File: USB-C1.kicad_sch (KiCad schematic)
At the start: 24 parts, among them J2 USB_C_Receptacle, J3 I2C_HD3SS3220, U3 HD3SS3220IRNHR, U4 TPS2068EDBVR, U5 TPD4E02B04DQA, U6 TPD4E02B04DQA, U7 TPD4E02B04DQA

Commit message: TPS25762 EEPROM connector added
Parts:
- renumbered R11 to R10, R12 to R11, R8 to R7, R9 to R8, R10 to R9
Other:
- title: (none) -> USB Hub
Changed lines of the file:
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@@
 	(generator_version "9.0")
 	(paper "A4")
+	(title_block
+		(title "USB Hub")
+	)
 	(rectangle
 		(start 15.24 13.97)
@@
 		(on_board yes)
 		(dnp no)
-		(property "Reference" "#PWR053"
+		(property "Reference" "#PWR052"
 			(at 184.15 162.56 0)
 			(effects
@@
 			(project "USB_hub"
 				(path "/a2586c28-95f1-49e6-9254-37d7a8473e53/9818f2bb-7888-47ed-88c0-ae123f59f09a"
-					(reference "#PWR053")
+					(reference "#PWR052")
 					(unit 1)
 				)
@@
 		(dnp no)
 		(fields_autoplaced yes)
-		(property "Reference" "#PWR041"
+		(property "Reference" "#PWR040"
 			(at 149.86 58.42 0)
 			(effects
@@
 			(project ""
 				(path "/a2586c28-95f1-49e6-9254-37d7a8473e53/9818f2bb-7888-47ed-88c0-ae123f59f09a"
-					(reference "#PWR041")
+					(reference "#PWR040")
 					(unit 1)
 				)
@@
 		(dnp no)
 		(fields_autoplaced yes)
-		(property "Reference" "R8"
+		(property "Reference" "R7"
 			(at 50.8 44.4499 0)
 			(effects
@@
 			(project ""
 				(path "/a2586c28-95f1-49e6-9254-37d7a8473e53/9818f2bb-7888-47ed-88c0-ae123f59f09a"
-					(reference "R8")
+					(reference "R7")
 					(unit 1)
 				)
@@
 		(dnp no)
 		(fields_autoplaced yes)
-		(property "Reference" "#PWR056"
+		(property "Reference" "#PWR055"
 			(at 25.4 194.31 0)
 			(effects
@@
 			(project "USB_hub"
 				(path "/a2586c28-95f1-49e6-9254-37d7a8473e53/9818f2bb-7888-47ed-88c0-ae123f59f09a"
-					(reference "#PWR056")
+					(reference "#PWR055")
 					(unit 1)
 				)
@@
 		(dnp no)
 		(fields_autoplaced yes)
-		(property "Reference" "#PWR047"
+		(property "Reference" "#PWR046"
 			(at 26.67 129.54 0)
 			(effects
@@
 			(project ""
 				(path "/a2586c28-95f1-49e6-9254-37d7a8473e53/9818f2bb-7888-47ed-88c0-ae123f59f09a"
-					(reference "#PWR047")
+					(reference "#PWR046")
 					(unit 1)
 				)
@@
 		(dnp no)
 		(fields_autoplaced yes)
-		(property "Reference" "#PWR037"
+		(property "Reference" "#PWR036"
 			(at 26.67 44.45 0)
 			(effects
@@
 			(project ""
 				(path "/a2586c28-95f1-49e6-9254-37d7a8473e53/9818f2bb-7888-47ed-88c0-ae123f59f09a"
-					(reference "#PWR037")
+					(reference "#PWR036")
 					(unit 1)
 				)
@@
 		(dnp no)
 		(fields_autoplaced yes)
-		(property "Reference" "#PWR040"
+		(property "Reference" "#PWR039"
 			(at 57.15 49.53 0)
 			(effects
@@
 			(project ""
 				(path "/a2586c28-95f1-49e6-9254-37d7a8473e53/9818f2bb-7888-47ed-88c0-ae123f59f09a"
-					(reference "#PWR040")
+					(reference "#PWR039")
 					(unit 1)
 				)
@@
 		(dnp no)
 		(fields_autoplaced yes)
-		(property "Reference" "R9"
+		(property "Reference" "R8"
 			(at 43.18 49.53 90)
 			(effects
@@
 			(project ""
 				(path "/a2586c28-95f1-49e6-9254-37d7a8473e53/9818f2bb-7888-47ed-88c0-ae123f59f09a"
-					(reference "R9")
+					(reference "R8")
 					(unit 1)
 				)
@@
 		(dnp no)
 		(fields_autoplaced yes)
-		(property "Reference" "#PWR055"
+		(property "Reference" "#PWR054"
 			(at 262.89 163.83 0)
 			(effects
@@
 			(project "USB_hub"
 				(path "/a2586c28-95f1-49e6-9254-37d7a8473e53/9818f2bb-7888-47ed-88c0-ae123f59f09a"
-					(reference "#PWR055")
+					(reference "#PWR054")
 					(unit 1)
 				)
@@
 		(dnp no)
 		(fields_autoplaced yes)
-		(property "Reference" "#PWR038"
+		(property "Reference" "#PWR037"
 			(at 62.23 44.45 0)
 			(effects
@@
 			(project ""
 				(path "/a2586c28-95f1-49e6-9254-37d7a8473e53/9818f2bb-7888-47ed-88c0-ae123f59f09a"
-					(reference "#PWR038")
+					(reference "#PWR037")
 					(unit 1)
 				)
@@
 		(dnp no)
 		(fields_autoplaced yes)
-		(property "Reference" "#PWR039"
+		(property "Reference" "#PWR038"
 			(at 48.26 45.72 0)
 			(effects
@@
 			(project "USB_hub"
 				(path "/a2586c28-95f1-49e6-9254-37d7a8473e53/9818f2bb-7888-47ed-88c0-ae123f59f09a"
-					(reference "#PWR039")
+					(reference "#PWR038")
 					(unit 1)
 				)
@@
 		(dnp no)
 		(fields_autoplaced yes)
-		(property "Reference" "#PWR051"
+		(property "Reference" "#PWR050"
 			(at 73.66 143.51 0)
 			(effects
@@
 			(project ""
 				(path "/a2586c28-95f1-49e6-9254-37d7a8473e53/9818f2bb-7888-47ed-88c0-ae123f59f09a"
-					(reference "#PWR051")
+					(reference "#PWR050")
 					(unit 1)
 				)
@@
 		(dnp no)
 		(fields_autoplaced yes)
-		(property "Reference" "#PWR045"
+		(property "Reference" "#PWR044"
 			(at 135.89 95.25 0)
 			(effects
@@
 			(project ""
 				(path "/a2586c28-95f1-49e6-9254-37d7a8473e53/9818f2bb-7888-47ed-88c0-ae123f59f09a"
-					(reference "#PWR045")
+					(reference "#PWR044")
 					(unit 1)
 				)
@@
 		(dnp no)
 		(fields_autoplaced yes)
-		(property "Reference" "#PWR035"
+		(property "Reference" "#PWR034"
 			(at 26.67 27.94 0)
 			(effects
@@
 			(project "USB_hub"
 				(path "/a2586c28-95f1-49e6-9254-37d7a8473e53/9818f2bb-7888-47ed-88c0-ae123f59f09a"
-					(reference "#PWR035")
+					(reference "#PWR034")
 					(unit 1)
 				)
@@
 		(dnp no)
 		(fields_autoplaced yes)
-		(property "Reference" "#PWR046"
+		(property "Reference" "#PWR045"
 			(at 248.92 100.33 0)
 			(effects
@@
 			(project ""
 				(path "/a2586c28-95f1-49e6-9254-37d7a8473e53/9818f2bb-7888-47ed-88c0-ae123f59f09a"
-					(reference "#PWR046")
+					(reference "#PWR045")
 					(unit 1)
 				)
@@
 		(on_board yes)
 		(dnp no)
-		(property "Reference" "R11"
+		(property "Reference" "R10"
 			(at 45.212 69.596 90)
 			(effects
@@
 			(project ""
 				(path "/a2586c28-95f1-49e6-9254-37d7a8473e53/9818f2bb-7888-47ed-88c0-ae123f59f09a"
-					(reference "R11")
+					(reference "R10")
 					(unit 1)
 				)
@@
 		(on_board yes)
 		(dnp no)
-		(property "Reference" "#PWR043"
+		(property "Reference" "#PWR042"
 			(at 49.53 59.69 0)
 			(effects
@@
 			(project "USB_hub"
 				(path "/a2586c28-95f1-49e6-9254-37d7a8473e53/9818f2bb-7888-47ed-88c0-ae123f59f09a"
-					(reference "#PWR043")
+					(reference "#PWR042")
 					(unit 1)
 				)
@@
 		(dnp no)
 		(fields_autoplaced yes)
-		(property "Reference" "#PWR036"
+		(property "Reference" "#PWR035"
 			(at 228.6 27.94 0)
 			(effects
@@
 			(project ""
 				(path "/a2586c28-95f1-49e6-9254-37d7a8473e53/9818f2bb-7888-47ed-88c0-ae123f59f09a"
-					(reference "#PWR036")
+					(reference "#PWR035")
 					(unit 1)
 				)
@@
 		(dnp no)
 		(fields_autoplaced yes)
-		(property "Reference" "#PWR054"
+		(property "Reference" "#PWR053"
 			(at 222.25 163.83 0)
 			(effects
@@
 			(project "USB_hub"
 				(path "/a2586c28-95f1-49e6-9254-37d7a8473e53/9818f2bb-7888-47ed-88c0-ae123f59f09a"
-					(reference "#PWR054")
+					(reference "#PWR053")
 					(unit 1)
 				)
@@
 		(dnp no)
 		(fields_autoplaced yes)
-		(property "Reference" "#PWR049"
+		(property "Reference" "#PWR048"
 			(at 26.67 142.24 0)
 			(effects
@@
 			(project "USB_hub"
 				(path "/a2586c28-95f1-49e6-9254-37d7a8473e53/9818f2bb-7888-47ed-88c0-ae123f59f09a"
-					(reference "#PWR049")
+					(reference "#PWR048")
 					(unit 1)
 				)
@@
 		(dnp no)
 		(fields_autoplaced yes)
-		(property "Reference" "R12"
+		(property "Reference" "R11"
 			(at 78.74 130.8099 0)
 			(effects
@@
 			(project ""
 				(path "/a2586c28-95f1-49e6-9254-37d7a8473e53/9818f2bb-7888-47ed-88c0-ae123f59f09a"
-					(reference "R12")
+					(reference "R11")
 					(unit 1)
 				)
@@
 		(on_board yes)
 		(dnp no)
-		(property "Reference" "R10"
+		(property "Reference" "R9"
 			(at 45.212 64.516 90)
 			(effects
@@
 			(project "USB_hub"
 				(path "/a2586c28-95f1-49e6-9254-37d7a8473e53/9818f2bb-7888-47ed-88c0-ae123f59f09a"
-					(reference "R10")
+					(reference "R9")
 					(unit 1)
 				)
@@
 		(on_board yes)
 		(dnp no)
-		(property "Reference" "#PWR042"
+		(property "Reference" "#PWR041"
 			(at 36.83 57.15 0)
 			(effects
@@
 			(project ""
 				(path "/a2586c28-95f1-49e6-9254-37d7a8473e53/9818f2bb-7888-47ed-88c0-ae123f59f09a"
-					(reference "#PWR042")
+					(reference "#PWR041")
 					(unit 1)
 				)
@@
 		(dnp no)
 		(fields_autoplaced yes)
-		(property "Reference" "#PWR044"
+		(property "Reference" "#PWR043"
 			(at 38.1 73.66 0)
 			(effects
@@
 			(project "USB_hub"
 				(path "/a2586c28-95f1-49e6-9254-37d7a8473e53/9818f2bb-7888-47ed-88c0-ae123f59f09a"
-					(reference "#PWR044")
+					(reference "#PWR043")
 					(unit 1)
 				)
@@
 		(dnp no)
 		(fields_autoplaced yes)
-		(property "Reference" "#PWR050"
+		(property "Reference" "#PWR049"
 			(at 36.83 142.24 0)
 			(effects
@@
 			(project "USB_hub"
 				(path "/a2586c28-95f1-49e6-9254-37d7a8473e53/9818f2bb-7888-47ed-88c0-ae123f59f09a"
-					(reference "#PWR050")
+					(reference "#PWR049")
 					(unit 1)
 				)
@@
 		(dnp no)
 		(fields_autoplaced yes)
-		(property "Reference" "#PWR052"
+		(property "Reference" "#PWR051"
 			(at 91.44 143.51 0)
 			(effects
@@
 			(project "USB_hub"
 				(path "/a2586c28-95f1-49e6-9254-37d7a8473e53/9818f2bb-7888-47ed-88c0-ae123f59f09a"
-					(reference "#PWR052")
+					(reference "#PWR051")
 					(unit 1)
 				)
@@
 		(dnp no)
 		(fields_autoplaced yes)
-		(property "Reference" "#PWR048"
+		(property "Reference" "#PWR047"
 			(at 91.44 133.35 0)
 			(effects
@@
 			(project "USB_hub"
 				(path "/a2586c28-95f1-49e6-9254-37d7a8473e53/9818f2bb-7888-47ed-88c0-ae123f59f09a"
-					(reference "#PWR048")
+					(reference "#PWR047")
 					(unit 1)
 				)

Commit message: deleted duplicated capacitor
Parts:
- C22, C28, C30: footprint (none) -> Capacitor_THT:C_Radial_D10.0mm_H16.0mm_P5.00mm
- C23, C24, C25, C26, C27, C29: footprint (none) -> Capacitor_SMD:C_0402_1005Metric
- J2: footprint (none) -> Connector_USB:USB_C_Receptacle_Amphenol_12401610E4-2A
- J3: footprint (none) -> Connector_PinHeader_1.27mm:PinHeader_1x03_P1.27mm_Vertical
- JP1: footprint (none) -> Jumper:SolderJumper-2_P1.3mm_Open_Pad1.0x1.5mm
- R10, R11, R7, R8, R9: footprint (none) -> Resistor_SMD:R_0603_1608Metric
- TP1, TP2: footprint (none) -> TestPoint:TestPoint_2Pads_Pitch5.08mm_Drill1.3mm
- U3: footprint RNH0030A -> footprints:RNH0030A
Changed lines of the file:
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@@
 			)
 		)
-		(property "Footprint" ""
+		(property "Footprint" "Capacitor_SMD:C_0402_1005Metric"
 			(at 134.62 60.96 0)
 			(effects
@@
 			)
 		)
-		(property "Footprint" ""
+		(property "Footprint" "Resistor_SMD:R_0603_1608Metric"
 			(at 50.038 45.72 90)
 			(effects
@@
 			)
 		)
-		(property "Footprint" ""
+		(property "Footprint" "TestPoint:TestPoint_2Pads_Pitch5.08mm_Drill1.3mm"
 			(at 22.86 163.83 0)
 			(effects
@@
 			)
 		)
-		(property "Footprint" ""
+		(property "Footprint" "Connector_PinHeader_1.27mm:PinHeader_1x03_P1.27mm_Vertical"
 			(at 21.59 175.26 0)
 			(effects
@@
 			)
 		)
-		(property "Footprint" ""
+		(property "Footprint" "Capacitor_SMD:C_0402_1005Metric"
 			(at 143.51 63.5 0)
 			(effects
@@
 			)
 		)
-		(property "Footprint" ""
+		(property "Footprint" "Capacitor_THT:C_Radial_D10.0mm_H16.0mm_P5.00mm"
 			(at 26.67 133.35 0)
 			(effects
@@
 			)
 		)
-		(property "Footprint" ""
+		(property "Footprint" "Resistor_SMD:R_0603_1608Metric"
 			(at 43.18 57.658 90)
 			(effects
@@
 			)
 		)
-		(property "Footprint" ""
+		(property "Footprint" "Jumper:SolderJumper-2_P1.3mm_Open_Pad1.0x1.5mm"
 			(at 31.75 187.96 0)
 			(effects
@@
 			)
 		)
-		(property "Footprint" ""
+		(property "Footprint" "Capacitor_SMD:C_0402_1005Metric"
 			(at 36.83 133.35 0)
 			(effects
@@
 			)
 		)
-		(property "Footprint" ""
+		(property "Footprint" "TestPoint:TestPoint_2Pads_Pitch5.08mm_Drill1.3mm"
 			(at 22.86 156.21 0)
 			(effects
@@
 			)
 		)
-		(property "Footprint" ""
+		(property "Footprint" "Resistor_SMD:R_0603_1608Metric"
 			(at 49.53 72.898 90)
 			(effects
@@
 			)
 		)
-		(property "Footprint" ""
+		(property "Footprint" "Connector_USB:USB_C_Receptacle_Amphenol_12401610E4-2A"
 			(at 245.11 50.8 0)
 			(effects
@@
 			)
 		)
-		(property "Footprint" ""
+		(property "Footprint" "Capacitor_SMD:C_0402_1005Metric"
 			(at 143.51 76.2 0)
 			(effects
@@
 			)
 		)
-		(property "Footprint" ""
+		(property "Footprint" "Capacitor_THT:C_Radial_D10.0mm_H16.0mm_P5.00mm"
 			(at 21.2852 34.29 0)
 			(effects
@@
 			)
 		)
-		(property "Footprint" ""
+		(property "Footprint" "Resistor_SMD:R_0603_1608Metric"
 			(at 81.28 132.08 0)
 			(effects
@@
 			)
 		)
-		(property "Footprint" ""
+		(property "Footprint" "Capacitor_SMD:C_0402_1005Metric"
 			(at 33.9852 34.29 0)
 			(effects
@@
 			)
 		)
-		(property "Footprint" ""
+		(property "Footprint" "Capacitor_THT:C_Radial_D10.0mm_H16.0mm_P5.00mm"
 			(at 91.44 133.35 0)
 			(effects
@@
 			)
 		)
-		(property "Footprint" "RNH0030A"
+		(property "Footprint" "footprints:RNH0030A"
 			(at 96.52 66.04 0)
 			(effects
@@
 			)
 		)
-		(property "Footprint" ""
+		(property "Footprint" "Resistor_SMD:R_0603_1608Metric"
 			(at 49.53 67.818 90)
 			(effects
@@
 			)
 		)
-		(property "Footprint" ""
+		(property "Footprint" "Capacitor_SMD:C_0402_1005Metric"
 			(at 134.62 73.66 0)
 			(effects

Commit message: Minor fixes
Fixed unclear labelling of buses
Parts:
- R10, R11, R7, R8, R9: footprint Resistor_SMD:R_0603_1608Metric -> Resistor_SMD:R_0402_1005Metric
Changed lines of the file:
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@@
 			)
 		)
-		(property "Footprint" "Resistor_SMD:R_0603_1608Metric"
+		(property "Footprint" "Resistor_SMD:R_0402_1005Metric"
 			(at 50.038 45.72 90)
 			(effects
@@
 			)
 		)
-		(property "Footprint" "Resistor_SMD:R_0603_1608Metric"
+		(property "Footprint" "Resistor_SMD:R_0402_1005Metric"
 			(at 43.18 57.658 90)
 			(effects
@@
 			)
 		)
-		(property "Footprint" "Resistor_SMD:R_0603_1608Metric"
+		(property "Footprint" "Resistor_SMD:R_0402_1005Metric"
 			(at 49.53 72.898 90)
 			(effects
@@
 			)
 		)
-		(property "Footprint" "Resistor_SMD:R_0603_1608Metric"
+		(property "Footprint" "Resistor_SMD:R_0402_1005Metric"
 			(at 81.28 132.08 0)
 			(effects
@@
 			)
 		)
-		(property "Footprint" "Resistor_SMD:R_0603_1608Metric"
+		(property "Footprint" "Resistor_SMD:R_0402_1005Metric"
 			(at 49.53 67.818 90)
 			(effects

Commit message: Scheme fixes
Fixed wrong connection of SNS pin of U21
USB7206c symbol improved
R7's value fixed
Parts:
- added D9: LED, symbol Device:LED
- added R72: 5k, symbol Device:R
- added R73: 200k, symbol Device:R
- J3: symbol Connector:Conn_01x03_Pin -> Connector:Conn_01x04_Pin
- R7: value 900 -> 900k
- U5, U6, U7: symbol Power_Protection:TPD4E02B04DQA -> Snapeda:TPD4E02B04DQA
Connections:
- net +3V3: now also R73.1
- net +5V: now also R11.1, R72.2
- net GND: now also J3.4 (Pin_4)
- net ID: now also R73.2
- net USB-C1.CC1: now also U5.10 (NC)
- net USB-C1.CC2: now also U5.9 (NC)
- net USB-C1.D+: now also U5.6 (NC)
- net USB-C1.D-: now also U5.7 (NC)
- net USB-C1.RX1+: now also U7.9 (NC)
- net USB-C1.RX1-: now also U7.10 (NC)
- net USB-C1.RX2+: now also U6.9 (NC)
- net USB-C1.RX2-: now also U6.10 (NC)
- net USB-C1.TX1+: now also U7.6 (NC)
- net USB-C1.TX1-: now also U7.7 (NC)
- net USB-C1.TX2+: now also U6.6 (NC)
- net USB-C1.TX2-: now also U6.7 (NC)
- net VBUS_C1: no longer R11.1
- net ~{FLT}: now reaches R11.2, U4.3 (~{FLT})
- net ~{FLT}: now also D9.1 (K)
- new net: D9.2 (A), R72.1
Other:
- note added: "TPS2068 Fault Indicator"
- moved on the sheet: R11

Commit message: MCP19035 changed to MP8795
TPS7A4701xRGW to AP7361C-33E
Led Indicator added
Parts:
- added D13: ESD441DPLR, EasyEDA:X2SON-2_L0.6-W0.3-P0.35, symbol EasyEDA:ESD441DPLR
- added D14: GREEN, symbol Device:LED
- added R85, R86: 4.7k, symbol Device:R
- added R89: 1.5k, symbol Device:R
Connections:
- net +3V3: now also R85.1, R86.1
- net GND: now also D13.2 (A), D14.1 (K)
- net I2C_HD3SS3220.SCL: now also R85.2
- net I2C_HD3SS3220.SDA: now also R86.2
- net VBUS_C1: now also R89.1
- new net: D14.2 (A), R89.2
- new net VBUS-C1: D13.1 (C)
- no-connect marks 14 -> 2

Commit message: I2C Addresses added to scheme
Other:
- note added: "I2C Address 0x47"
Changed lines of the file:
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@@
+		)
+	)
+	(text "I2C Address 0x47"
+		(exclude_from_sim no)
+		(at 41.148 192.278 0)
+		(effects
+			(font
+				(size 1.27 1.27)
+			)
 		)
 	)

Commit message: Ferrite Breads added for 5V, TVS and ESD diodes added
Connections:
- net +5V renamed +5V_USB_C_SD
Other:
- moved on the sheet: D14, R89

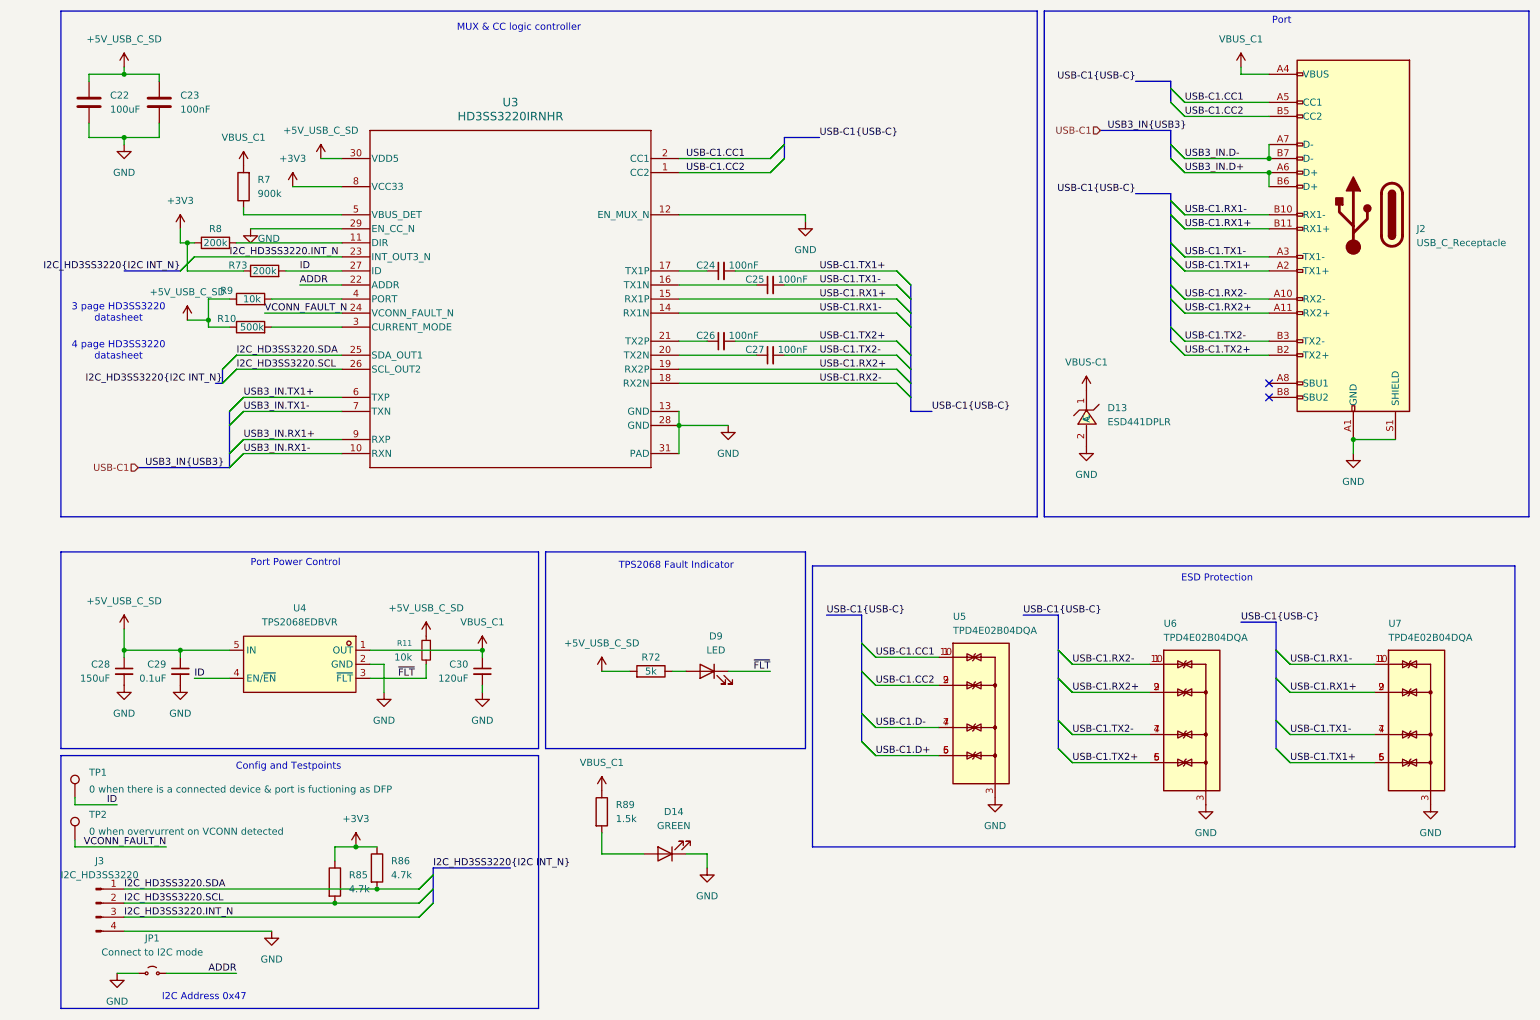
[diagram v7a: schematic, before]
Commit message: Ferrite bread filter for LDO and MIC23201, labelling improved
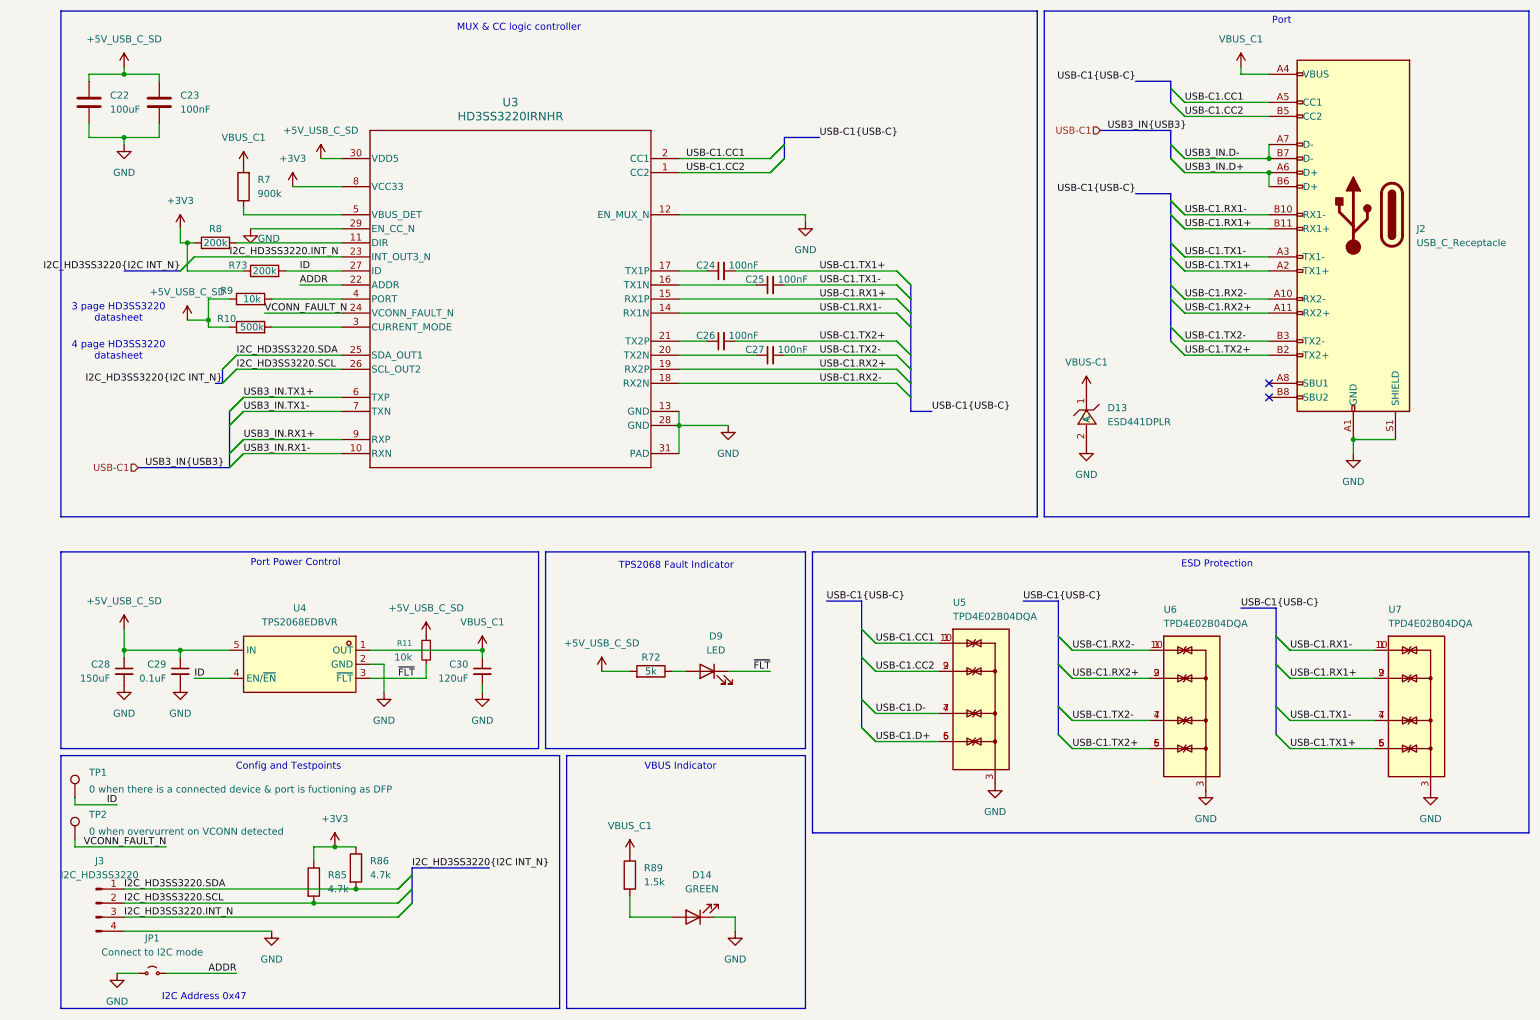
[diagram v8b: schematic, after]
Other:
- note added: "VBUS Indicator"
- moved on the sheet: D14, R85, R86, R89, U5, U6, U7
